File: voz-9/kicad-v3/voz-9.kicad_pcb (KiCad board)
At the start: 2 copper layers, 200 x 100 mm, 232 parts, among them J1 AMOUNT, J1 CUTOFF, J1 DRONE, J1 OSC A, J1 OSC B, J1 SHAPE, J1 SW A, J1 SW B, J2 DEPTH, J2 MODE, J2 RATE, J2 TREM, J3 F-BACK, J3 H1, J3 H2, J3 H3, J3 STACK, J3 TIME, J3 VOLUME, J3 WET, J4 A, J4 B, J4 FCV, J4 FILT, J4 IN, J4 VCV, J5 CLK, J5 ECV, J5 LFO, J5 RCV, J5 SEND, J6 GATE, J6 LED, J6 P4, J7 OSC IN, J7 PRE, J7 XLR IN, J8 XLR OUT, J9 HIGH, J9 LOW, J9 MID F, J9 MID G, Q1 MMBFJ201, Q2 MMBFJ201, Q3 MMBFJ201, Q4 MMBFJ201, Q5 MMBFJ201, Q6 MMBFJ201, Q7 MMBF5457, U1 NE5532DR, U2 TL072CDR, U3 TL072CDR, U4 ICL7660, U5 78M05, U6 PT2399, U7 PT2399, U8 PT2399, U9 TL072CDR

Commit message: Define a altura da placa v3 em 150 mm.
O contorno passa de 200 x 100 mm para 200 x 150 mm. Os pinos da interface e os furos M3 de baixo acompanham a base, com o mesmo recuo de antes.

Co-authored-by: Andrey <andreysenes@users.noreply.github.com>
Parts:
- moved C45 80.2 mm to (147.8, 32.5)
- moved C30 80.2 mm to (153.0, 32.5)
- moved R21 77.9 mm to (83.1, 20.8)
- moved H3 50.0 mm to (4.20, 145.8)
- moved H4 50.0 mm to (195.8, 145.8)
- moved J1 50.0 mm to (96.0, 134.0)
- moved J1 50.0 mm to (28.7, 126.0)
- moved J1 50.0 mm to (80.2, 134.0)
- moved J1 50.0 mm to (64.4, 126.0)
- moved J1 50.0 mm to (139.6, 126.0)
- moved J1 50.0 mm to (107.9, 126.0)
- moved J1 50.0 mm to (52.5, 126.0)
- moved J1 50.0 mm to (40.6, 126.0)
- moved J2 50.0 mm to (64.4, 142.0)
- moved J2 50.0 mm to (16.8, 142.0)
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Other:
- board size 200 x 100 mm -> 200 x 150 mm

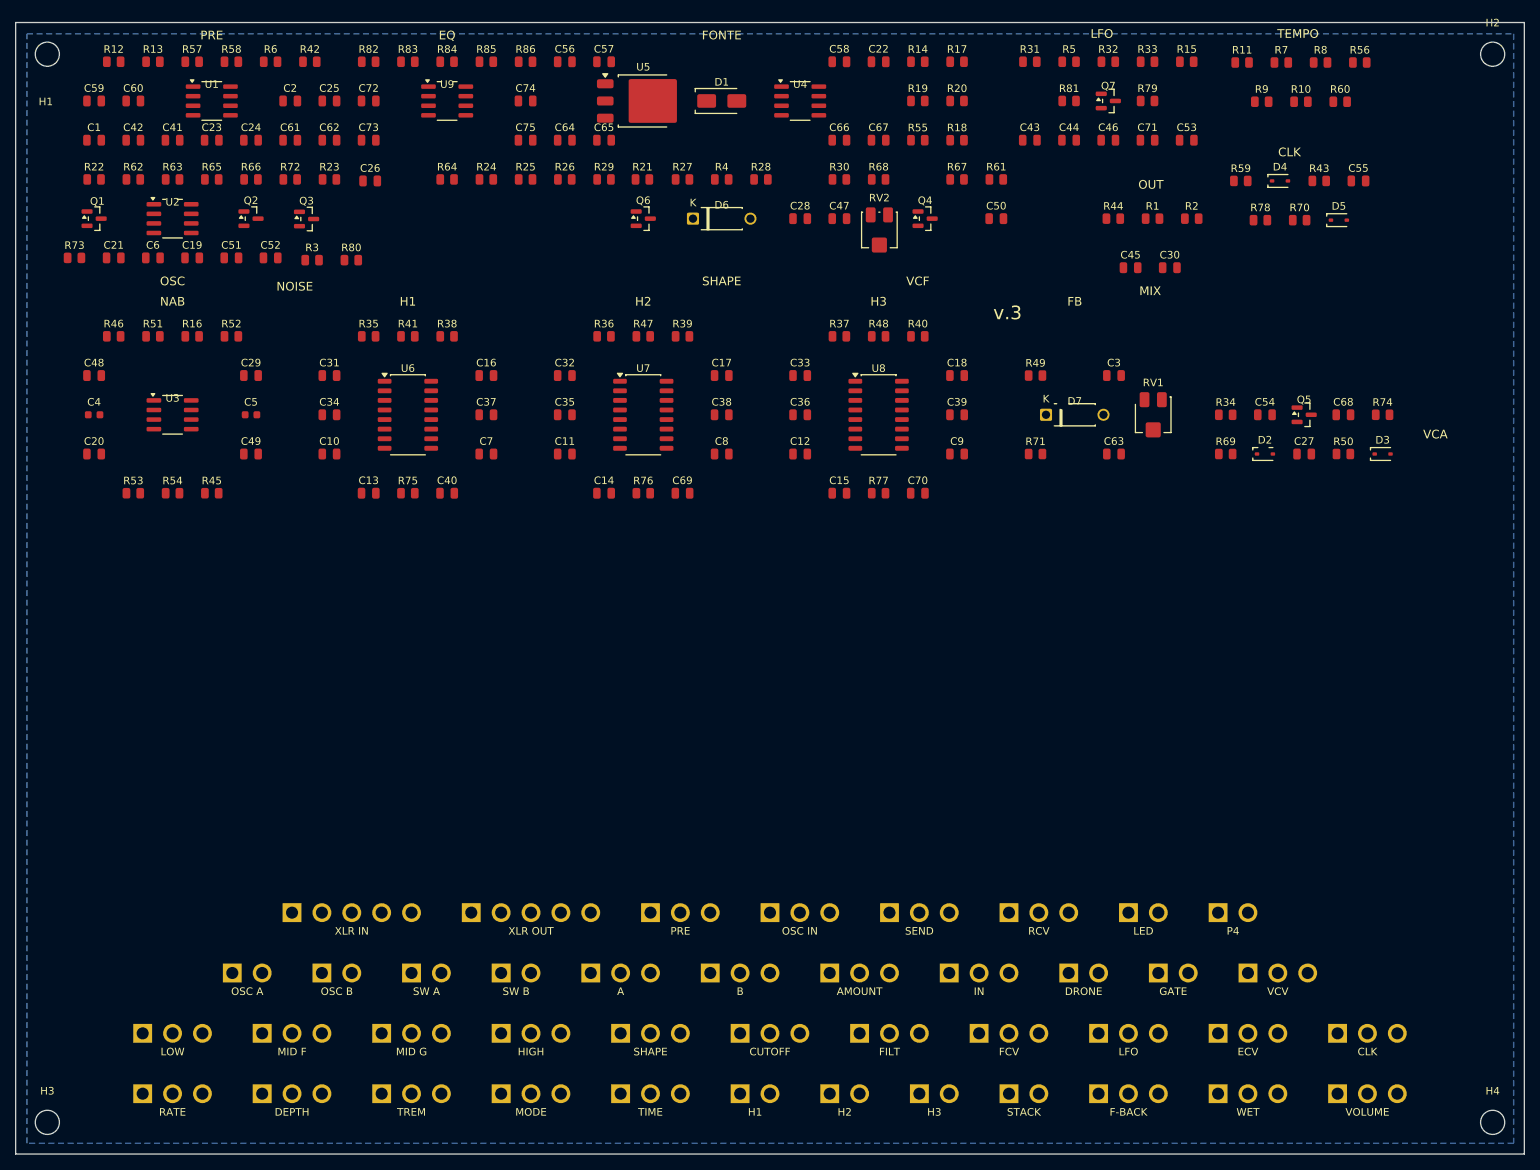
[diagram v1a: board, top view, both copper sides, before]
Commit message: Reorganiza os grupos da v3 na área útil.
O circuito sobe até perto dos pinos, com um canal entre cada faixa, na ordem do sinal. Os pads de cabo na base ficam no lugar.

Co-authored-by: Andrey <andreysenes@users.noreply.github.com>
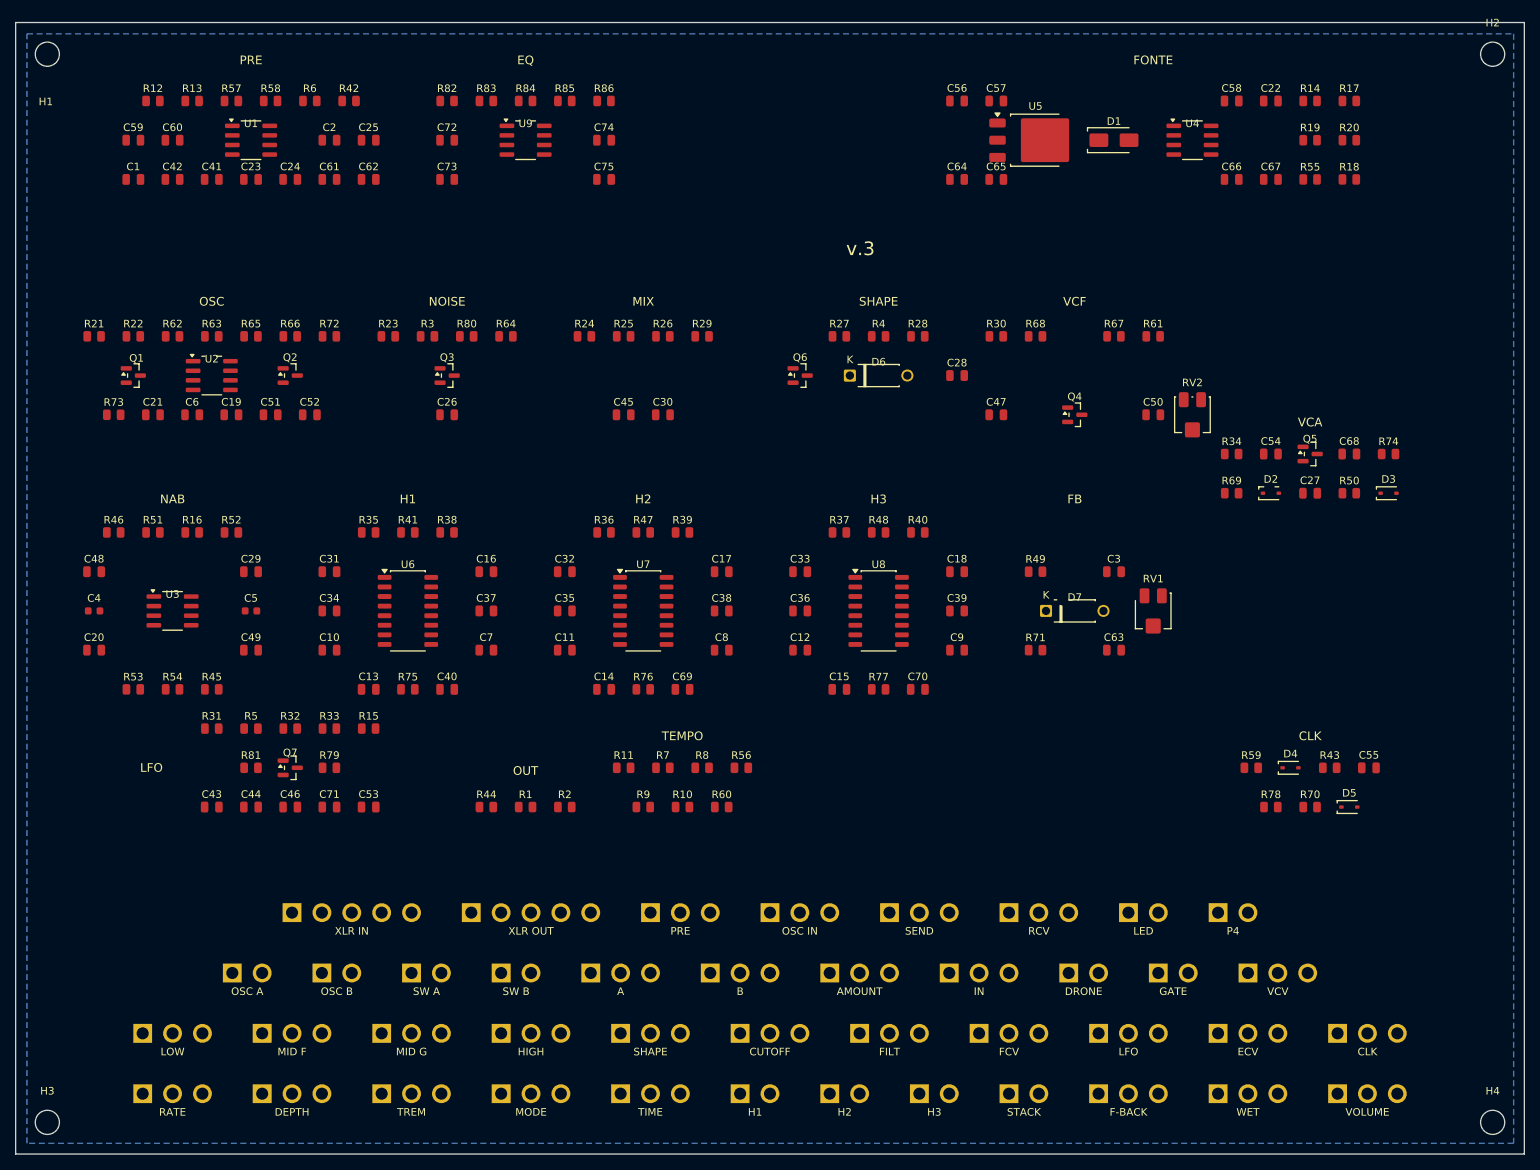
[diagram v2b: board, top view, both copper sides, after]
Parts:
- moved C71 139.9 mm to (41.6, 104.0)
- moved R33 139.9 mm to (41.6, 93.6)
- moved R79 139.9 mm to (41.6, 98.8)
- moved C43 139.9 mm to (26.0, 104.0)
- moved C44 139.9 mm to (31.2, 104.0)
- moved C46 139.9 mm to (36.4, 104.0)
- moved C53 139.9 mm to (46.8, 104.0)
- moved R15 139.9 mm to (46.8, 93.6)
- moved R5 139.9 mm to (31.2, 93.6)
- moved R81 139.9 mm to (31.2, 98.8)
- moved Q7 139.9 mm to (36.4, 98.8)
- moved R31 139.9 mm to (26.0, 93.6)
- moved R32 139.9 mm to (36.4, 93.6)
- moved R11 124.4 mm to (80.6, 98.8)
- moved R60 124.4 mm to (93.6, 104.0)
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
